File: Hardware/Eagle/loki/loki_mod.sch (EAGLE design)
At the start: 39 parts

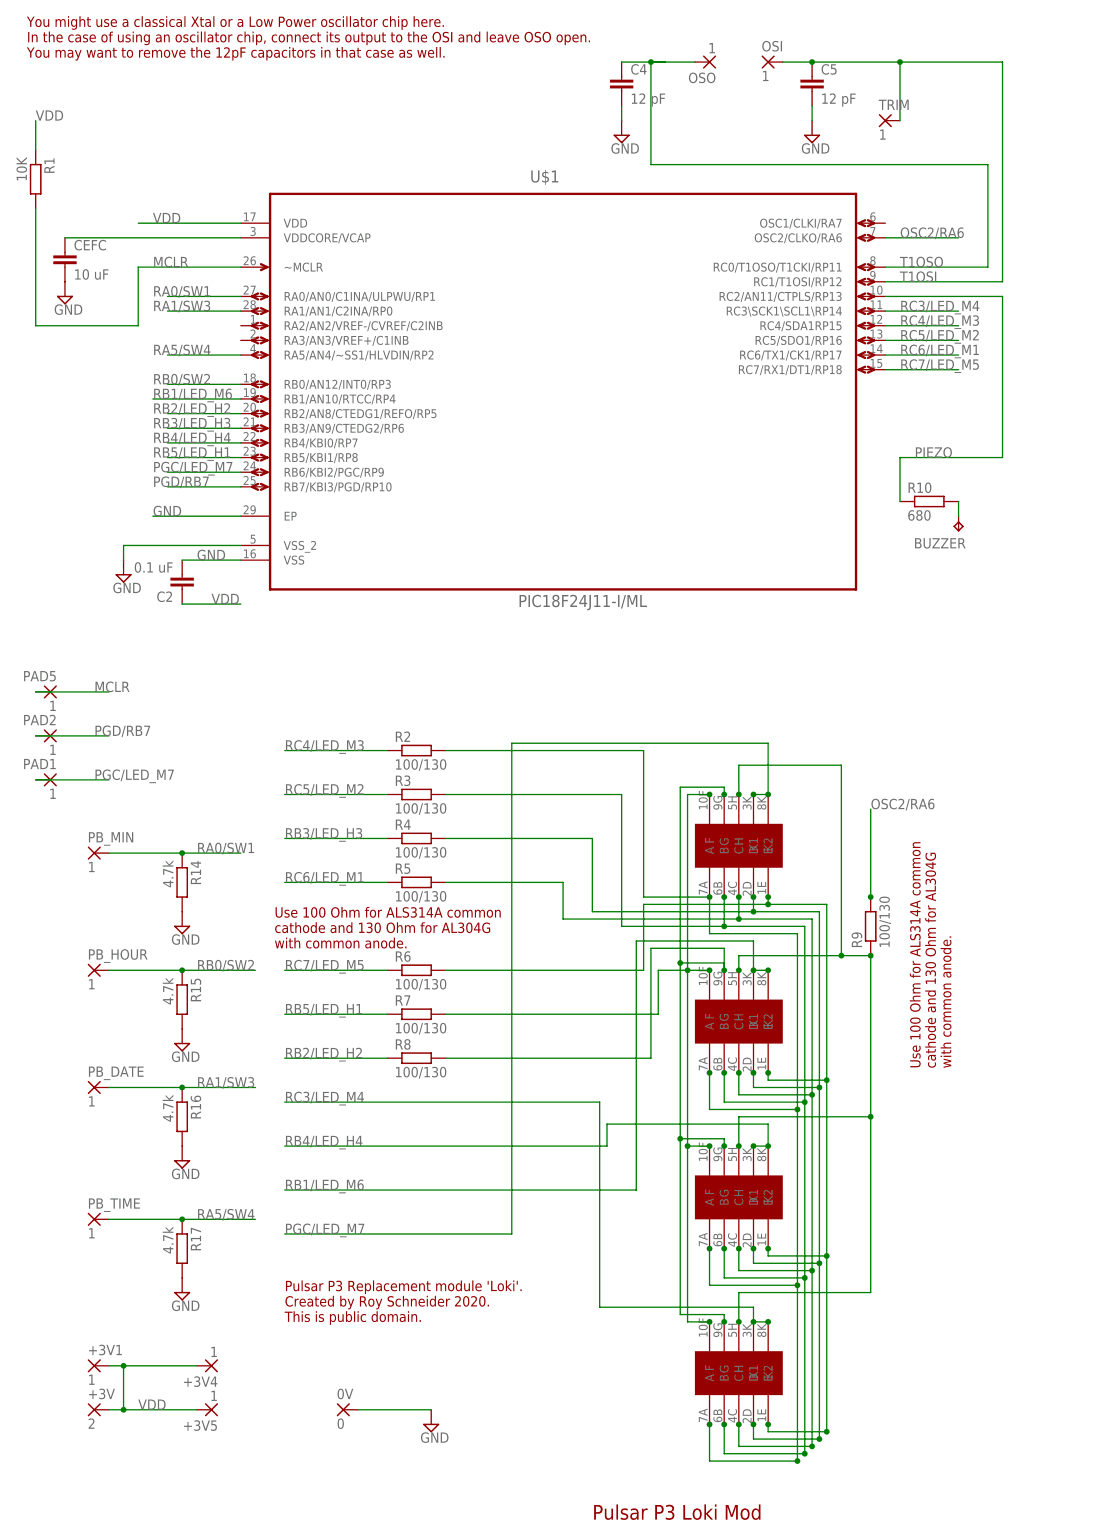
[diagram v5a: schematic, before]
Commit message: Optimized Odin and Loki layout.
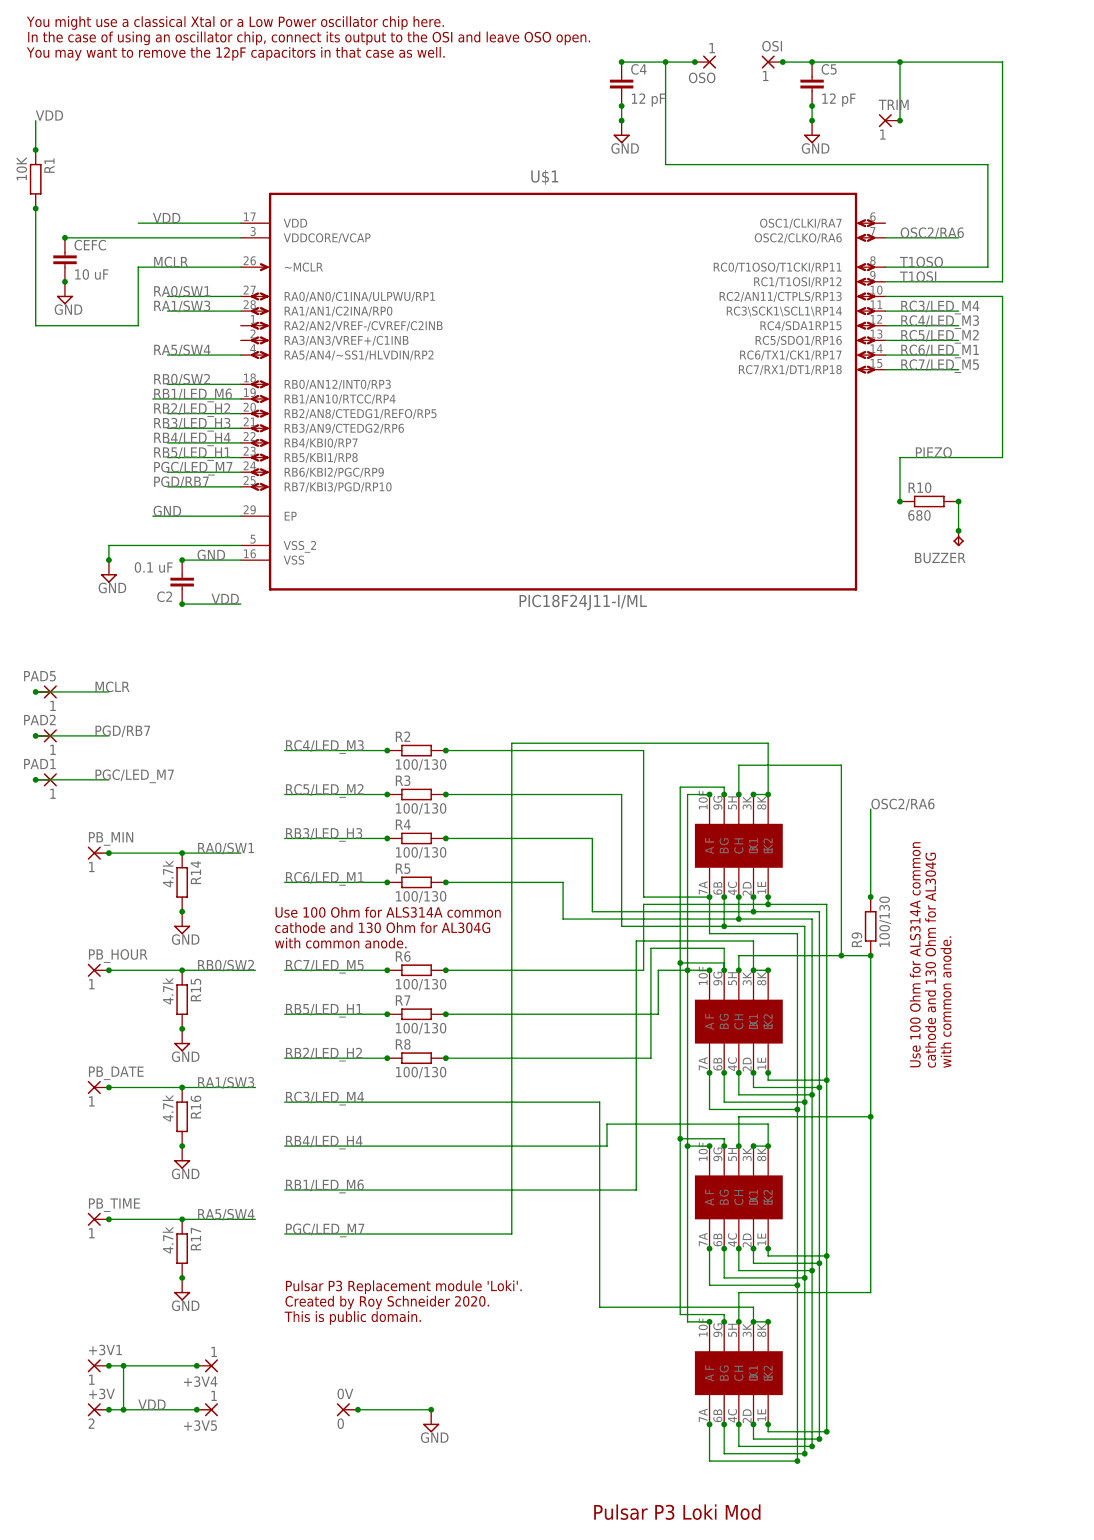
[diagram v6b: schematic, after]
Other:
- moved on the sheet: BUZZER
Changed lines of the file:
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@@
 <instance part="CEFC" gate="G$1" x="-114.3" y="109.22"/>
 <instance part="SUPPLY2" gate="GND" x="-114.3" y="101.6"/>
-<instance part="SUPPLY3" gate="GND" x="-104.14" y="53.34"/>
+<instance part="SUPPLY3" gate="GND" x="-106.68" y="53.34"/>
 <instance part="R2" gate="G$1" x="-53.34" y="22.86"/>
 <instance part="R3" gate="G$1" x="-53.34" y="15.24"/>
@@
 <instance part="R9" gate="G$1" x="25.4" y="-7.62" rot="R90"/>
 <instance part="R10" gate="G$1" x="35.56" y="66.04"/>
-<instance part="BUZZER" gate="G$1" x="40.64" y="60.96" rot="R180"/>
+<instance part="BUZZER" gate="G$1" x="40.64" y="58.42" rot="R180"/>
 </instances>
 <busses>
@@
 <pinref part="U$1" gate="A" pin="VSS_2"/>
 <pinref part="SUPPLY3" gate="GND" pin="GND"/>
-<wire x1="-83.82" y1="58.42" x2="-104.14" y2="58.42" width="0.1524" layer="91"/>
-<wire x1="-104.14" y1="58.42" x2="-104.14" y2="55.88" width="0.1524" layer="91"/>
+<wire x1="-83.82" y1="58.42" x2="-106.68" y2="58.42" width="0.1524" layer="91"/>
+<wire x1="-106.68" y1="58.42" x2="-106.68" y2="55.88" width="0.1524" layer="91"/>
+<junction x="-106.68" y="55.88"/>
 </segment>
 <segment>
 <pinref part="CEFC" gate="G$1" pin="2"/>
 <pinref part="SUPPLY2" gate="GND" pin="GND"/>
+<junction x="-114.3" y="104.14"/>
 </segment>
 <segment>
@@
 <wire x1="-83.82" y1="55.88" x2="-93.98" y2="55.88" width="0.1524" layer="91"/>
 <label x="-91.44" y="55.88" size="1.778" layer="95"/>
+<junction x="-93.98" y="55.88"/>
 </segment>
 <segment>
@@
 <wire x1="-63.5" y1="-91.44" x2="-50.8" y2="-91.44" width="0.1524" layer="91"/>
 <pinref part="0V" gate="1" pin="P"/>
+<junction x="-50.8" y="-91.44"/>
+<junction x="-63.5" y="-91.44"/>
 </segment>
 <segment>
@@
 <pinref part="SUPPLY7" gate="GND" pin="GND"/>
 <wire x1="-17.78" y1="134.62" x2="-17.78" y2="132.08" width="0.1524" layer="91"/>
+<junction x="-17.78" y="132.08"/>
+<junction x="-17.78" y="134.62"/>
 </segment>
 <segment>
@@
 <pinref part="SUPPLY8" gate="GND" pin="GND"/>
 <wire x1="15.24" y1="134.62" x2="15.24" y2="132.08" width="0.1524" layer="91"/>
+<junction x="15.24" y="134.62"/>
+<junction x="15.24" y="132.08"/>
 </segment>
 <segment>
 <pinref part="R14" gate="G$1" pin="2"/>
 <pinref part="SUPPLY1" gate="GND" pin="GND"/>
+<junction x="-93.98" y="-5.08"/>
 </segment>
 <segment>
 <pinref part="R15" gate="G$1" pin="2"/>
 <pinref part="SUPPLY5" gate="GND" pin="GND"/>
+<junction x="-93.98" y="-25.4"/>
 </segment>
 <segment>
 <pinref part="SUPPLY9" gate="GND" pin="GND"/>
 <pinref part="R16" gate="G$1" pin="2"/>
+<junction x="-93.98" y="-45.72"/>
 </segment>
 <segment>
 <pinref part="SUPPLY10" gate="GND" pin="GND"/>
 <pinref part="R17" gate="G$1" pin="2"/>
+<junction x="-93.98" y="-68.58"/>
 </segment>
 </net>
@@
 <pinref part="R1" gate="G$1" pin="2"/>
 <wire x1="-119.38" y1="96.52" x2="-119.38" y2="116.84" width="0.1524" layer="91"/>
+<junction x="-119.38" y="116.84"/>
 </segment>
 <segment>
@@
 <label x="-109.22" y="33.02" size="1.778" layer="95"/>
 <pinref part="PAD5" gate="1" pin="P"/>
+<junction x="-119.38" y="33.02"/>
 </segment>
 </net>
@@
 <wire x1="-106.68" y1="5.08" x2="-93.98" y2="5.08" width="0.1524" layer="91"/>
 <junction x="-93.98" y="5.08"/>
+<junction x="-106.68" y="5.08"/>
 </segment>
 <segment>
@@
 <wire x1="-106.68" y1="-15.24" x2="-93.98" y2="-15.24" width="0.1524" layer="91"/>
 <junction x="-93.98" y="-15.24"/>
+<junction x="-106.68" y="-15.24"/>
 </segment>
 <segment>
@@
 <junction x="-104.14" y="-91.44"/>
 <junction x="-104.14" y="-83.82"/>
+<junction x="-91.44" y="-91.44"/>
+<junction x="-91.44" y="-83.82"/>
+<junction x="-106.68" y="-83.82"/>
+<junction x="-106.68" y="-91.44"/>
 </segment>
 <segment>
@@
 <wire x1="-119.38" y1="127" x2="-119.38" y2="132.08" width="0.1524" layer="91"/>
 <label x="-119.38" y="132.08" size="1.778" layer="95"/>
+<junction x="-119.38" y="127"/>
 </segment>
 <segment>
@@
 <wire x1="-93.98" y1="48.26" x2="-83.82" y2="48.26" width="0.1524" layer="91"/>
 <label x="-88.9" y="48.26" size="1.778" layer="95"/>
+<junction x="-93.98" y="48.26"/>
 </segment>
 </net>
@@
 <wire x1="-58.42" y1="-30.48" x2="-76.2" y2="-30.48" width="0.1524" layer="91"/>
 <label x="-76.2" y="-30.48" size="1.778" layer="95"/>
+<junction x="-58.42" y="-30.48"/>
 </segment>
 </net>
@@
 <wire x1="-58.42" y1="7.62" x2="-76.2" y2="7.62" width="0.1524" layer="91"/>
 <label x="-76.2" y="7.62" size="1.778" layer="95"/>
+<junction x="-58.42" y="7.62"/>
 </segment>
 </net>
@@
 <wire x1="-58.42" y1="22.86" x2="-76.2" y2="22.86" width="0.1524" layer="91"/>
 <label x="-76.2" y="22.86" size="1.778" layer="95"/>
+<junction x="-58.42" y="22.86"/>
 </segment>
 </net>
@@
 <wire x1="-58.42" y1="15.24" x2="-76.2" y2="15.24" width="0.1524" layer="91"/>
 <label x="-76.2" y="15.24" size="1.778" layer="95"/>
+<junction x="-58.42" y="15.24"/>
 </segment>
 </net>
@@
 <wire x1="-58.42" y1="0" x2="-76.2" y2="0" width="0.1524" layer="91"/>
 <label x="-76.2" y="0" size="1.778" layer="95"/>
+<junction x="-58.42" y="0"/>
 </segment>
 </net>
@@
 <wire x1="-58.42" y1="-15.24" x2="-76.2" y2="-15.24" width="0.1524" layer="91"/>
 <label x="-76.2" y="-15.24" size="1.778" layer="95"/>
+<junction x="-58.42" y="-15.24"/>
 </segment>
 </net>
@@
 <wire x1="-58.42" y1="-22.86" x2="-76.2" y2="-22.86" width="0.1524" layer="91"/>
 <label x="-76.2" y="-22.86" size="1.778" layer="95"/>
+<junction x="-58.42" y="-22.86"/>
 </segment>
 </net>
@@
 <label x="-109.22" y="17.78" size="1.778" layer="95"/>
 <pinref part="PAD1" gate="1" pin="P"/>
+<junction x="-119.38" y="17.78"/>
 </segment>
 </net>
@@
 <label x="-109.22" y="25.4" size="1.778" layer="95"/>
 <pinref part="PAD2" gate="1" pin="P"/>
+<junction x="-119.38" y="25.4"/>
 </segment>
 </net>
@@
 <wire x1="45.72" y1="106.68" x2="45.72" y2="124.46" width="0.1524" layer="91"/>
 <pinref part="C4" gate="G$1" pin="1"/>
-<wire x1="-10.16" y1="142.24" x2="-12.7" y2="142.24" width="0.1524" layer="91"/>
-<wire x1="-12.7" y1="142.24" x2="-17.78" y2="142.24" width="0.1524" layer="91"/>
-<wire x1="-12.7" y1="124.46" x2="-12.7" y2="142.24" width="0.1524" layer="91"/>
-<junction x="-12.7" y="142.24"/>
-<wire x1="45.72" y1="124.46" x2="-12.7" y2="124.46" width="0.1524" layer="91"/>
+<wire x1="-10.16" y1="142.24" x2="-17.78" y2="142.24" width="0.1524" layer="91"/>
+<wire x1="-10.16" y1="124.46" x2="-10.16" y2="142.24" width="0.1524" layer="91"/>
+<junction x="-10.16" y="142.24"/>
+<wire x1="45.72" y1="124.46" x2="-10.16" y2="124.46" width="0.1524" layer="91"/>
 <pinref part="OSO" gate="1" pin="P"/>
-<wire x1="-12.7" y1="142.24" x2="-5.08" y2="142.24" width="0.1524" layer="91"/>
+<wire x1="-10.16" y1="142.24" x2="-5.08" y2="142.24" width="0.1524" layer="91"/>
+<junction x="-17.78" y="142.24"/>
+<junction x="-5.08" y="142.24"/>
 </segment>
 </net>
@@
 <wire x1="30.48" y1="132.08" x2="30.48" y2="142.24" width="0.1524" layer="91"/>
 <junction x="30.48" y="142.24"/>
+<junction x="30.48" y="132.08"/>
+<junction x="10.16" y="142.24"/>
 </segment>
 </net>
@@
 <wire x1="-93.98" y1="-35.56" x2="-81.28" y2="-35.56" width="0.1524" layer="91"/>
 <label x="-91.44" y="-35.56" size="1.778" layer="95"/>
+<junction x="-106.68" y="-35.56"/>
 </segment>
 </net>
@@
 <pinref part="CEFC" gate="G$1" pin="1"/>
 <wire x1="-83.82" y1="111.76" x2="-114.3" y2="111.76" width="0.1524" layer="91"/>
+<junction x="-114.3" y="111.76"/>
 </segment>
 </net>
@@
 <junction x="-93.98" y="-58.42"/>
 <label x="-91.44" y="-58.42" size="1.778" layer="95"/>
+<junction x="-106.68" y="-58.42"/>
 </segment>
 </net>
@@
 <junction x="-2.54" y="-45.72"/>
 <junction x="-2.54" y="-76.2"/>
+<junction x="-48.26" y="-22.86"/>
 </segment>
 </net>
@@
 <junction x="0" y="-45.72"/>
 <junction x="0" y="-76.2"/>
+<junction x="-48.26" y="-30.48"/>
 </segment>
 </net>
@@
 <junction x="-2.54" y="-63.5"/>
 <junction x="-2.54" y="-93.98"/>
+<junction x="-48.26" y="22.86"/>
 </segment>
 </net>
@@
 <junction x="0" y="-93.98"/>
 <junction x="0" y="-7.62"/>
+<junction x="-48.26" y="15.24"/>
 </segment>
 </net>
@@
 <junction x="2.54" y="-93.98"/>
 <junction x="2.54" y="-6.35"/>
+<junction x="-48.26" y="0"/>
 </segment>
 </net>
@@
 <junction x="5.08" y="-93.98"/>
 <junction x="5.08" y="-5.08"/>
+<junction x="-48.26" y="7.62"/>
 </segment>
 </net>
@@
 <junction x="7.62" y="-93.98"/>
 <junction x="7.62" y="-3.81"/>
+<junction x="-48.26" y="-15.24"/>
 </segment>
 </net>
@@
 <wire x1="30.48" y1="73.66" x2="30.48" y2="66.04" width="0.1524" layer="91"/>
 <pinref part="R10" gate="G$1" pin="1"/>
+<junction x="30.48" y="66.04"/>
 </segment>
 </net>
@@
 <pinref part="BUZZER" gate="G$1" pin="TP"/>
 <pinref part="R10" gate="G$1" pin="2"/>
-<wire x1="40.64" y1="63.5" x2="40.64" y2="66.04" width="0.1524" layer="91"/>
-</segment>
-</net>
+<wire x1="40.64" y1="60.96" x2="40.64" y2="66.04" width="0.1524" layer="91"/>
+<junction x="40.64" y="66.04"/>
+<junction x="40.64" y="60.96"/>
+</segment>
+</net>

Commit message: Reviewed boards and code.
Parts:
- R10: value 680 -> 470
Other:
- note added: "Do not use less than 10µF here!"
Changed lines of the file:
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@@
 <part name="1M" library="l104g" deviceset="L104G" device=""/>
 <part name="R9" library="resistor" deviceset="R-EU_" device="R0402" value="100/130"/>
-<part name="R10" library="resistor" deviceset="R-EU_" device="R0402" value="680"/>
+<part name="R10" library="resistor" deviceset="R-EU_" device="R0402" value="470"/>
 <part name="BUZZER" library="testpad" deviceset="TP" device="TP06SQ"/>
 </parts>
@@
 cathode and 130 Ohm for AL304G
 with common anode.</text>
+<text x="-118.364" y="87.122" size="1.778" layer="94">Do not use
+less than
+10µF here!</text>
 </plain>
 <instances>

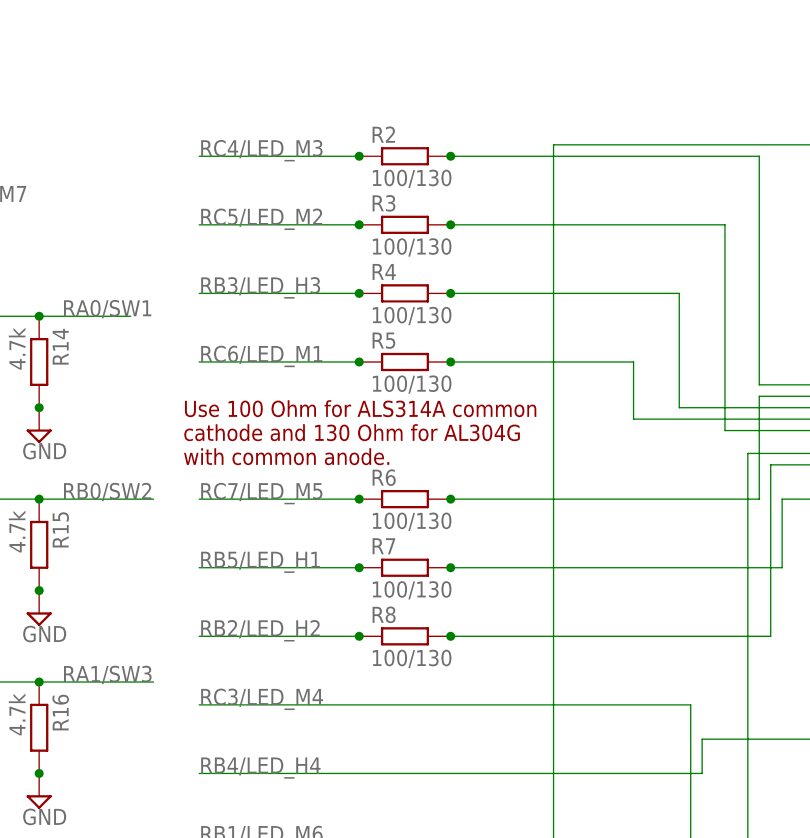
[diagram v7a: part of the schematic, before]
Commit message: Updated schematics comments.
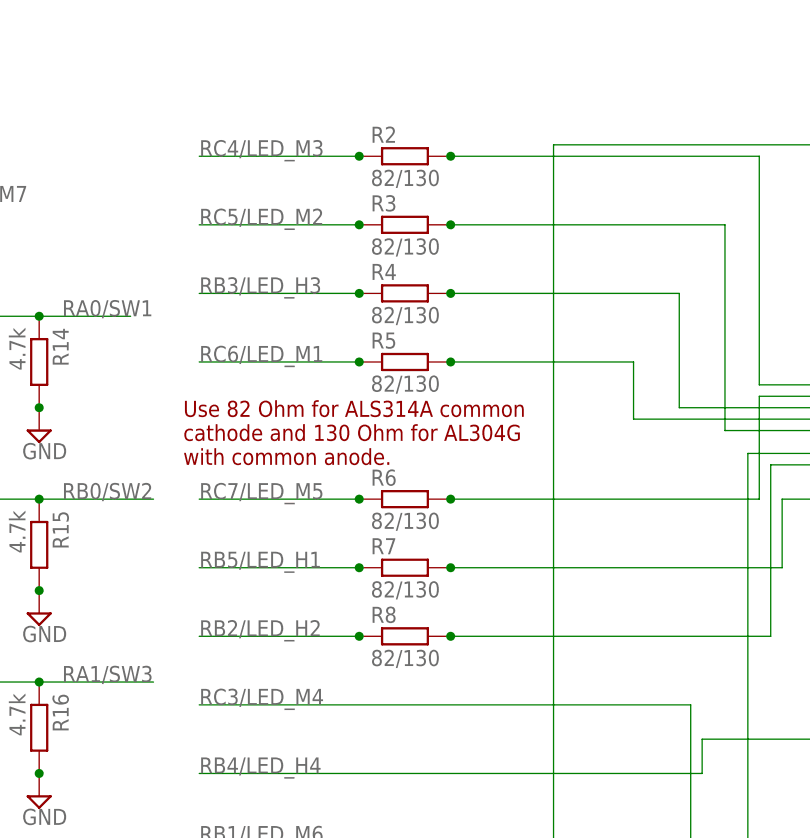
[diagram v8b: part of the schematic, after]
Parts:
- R2, R3, R4, R5, R6, R7, R8: value 100/130 -> 82/130
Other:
- note added: "Use 82 Ohm for ALS314A common cathode and 130 Ohm for AL304G with common anode."
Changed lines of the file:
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@@
 <part name="SUPPLY2" library="supply2" deviceset="GND" device=""/>
 <part name="SUPPLY3" library="supply2" deviceset="GND" device=""/>
-<part name="R2" library="resistor" deviceset="R-EU_" device="R0402" value="100/130"/>
-<part name="R3" library="resistor" deviceset="R-EU_" device="R0402" value="100/130"/>
-<part name="R4" library="resistor" deviceset="R-EU_" device="R0402" value="100/130"/>
-<part name="R5" library="resistor" deviceset="R-EU_" device="R0402" value="100/130"/>
-<part name="R6" library="resistor" deviceset="R-EU_" device="R0402" value="100/130"/>
-<part name="R7" library="resistor" deviceset="R-EU_" device="R0402" value="100/130"/>
-<part name="R8" library="resistor" deviceset="R-EU_" device="R0402" value="100/130"/>
+<part name="R2" library="resistor" deviceset="R-EU_" device="R0402" value="82/130"/>
+<part name="R3" library="resistor" deviceset="R-EU_" device="R0402" value="82/130"/>
+<part name="R4" library="resistor" deviceset="R-EU_" device="R0402" value="82/130"/>
+<part name="R5" library="resistor" deviceset="R-EU_" device="R0402" value="82/130"/>
+<part name="R6" library="resistor" deviceset="R-EU_" device="R0402" value="82/130"/>
+<part name="R7" library="resistor" deviceset="R-EU_" device="R0402" value="82/130"/>
+<part name="R8" library="resistor" deviceset="R-EU_" device="R0402" value="82/130"/>
 <part name="R14" library="resistor" deviceset="R-EU_" device="R0402" value="4.7k"/>
 <part name="R15" library="resistor" deviceset="R-EU_" device="R0402" value="4.7k"/>
@@
 This is public domain.</text>
 <text x="-22.86" y="-110.49" size="2.54" layer="94" font="vector">Pulsar P3 Loki Mod</text>
-<text x="-77.978" y="-11.43" size="1.778" layer="94">Use 100 Ohm for ALS314A common
+<text x="-77.978" y="-11.43" size="1.778" layer="94">Use 82 Ohm for ALS314A common
 cathode and 130 Ohm for AL304G
 with common anode.</text>
